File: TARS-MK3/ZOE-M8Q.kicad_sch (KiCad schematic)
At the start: 3 parts, among them U8001 ZOE-M8Q, X8001 SMACONNECTOR

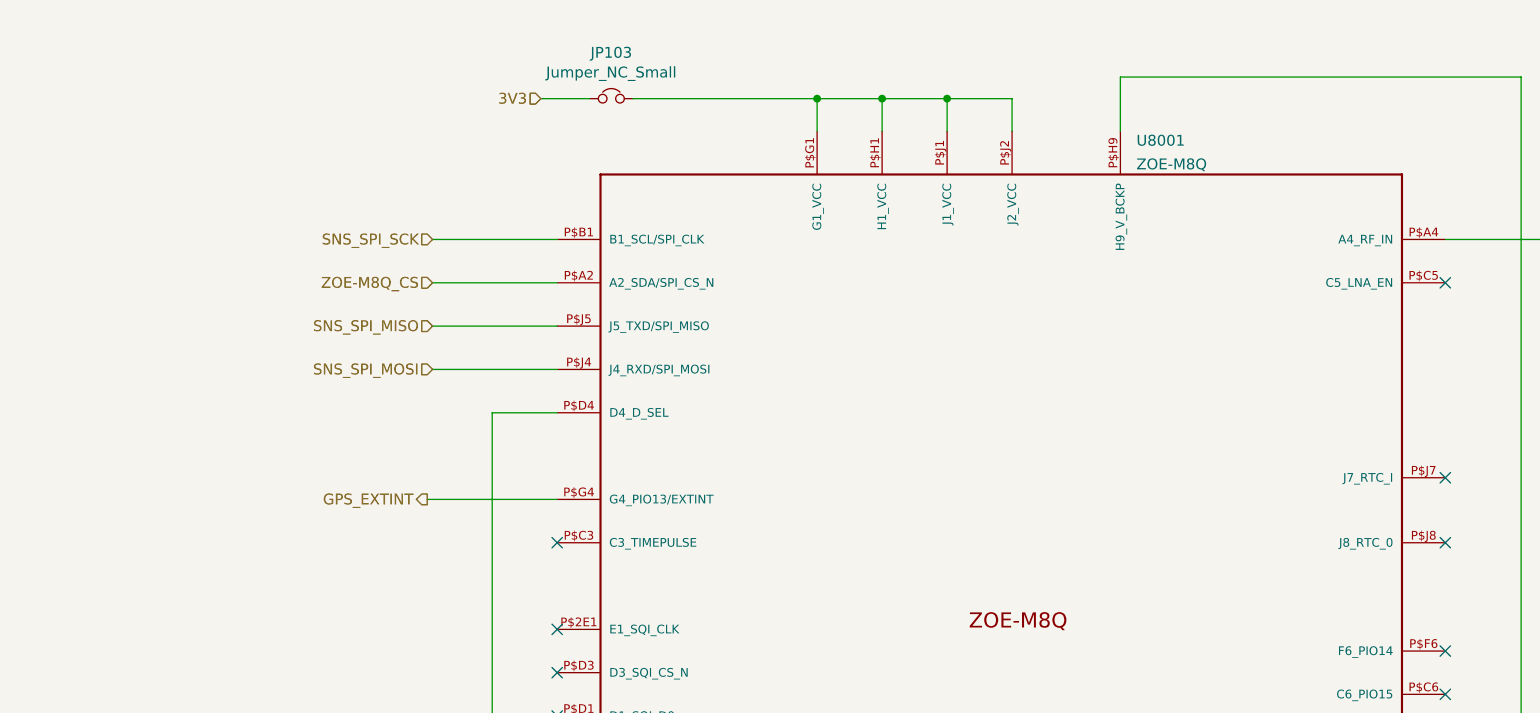
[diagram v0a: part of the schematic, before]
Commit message: added UART connections to ZOE m8q and slightly changed sensor suite pinout, also added 3V battery backup option should we want it
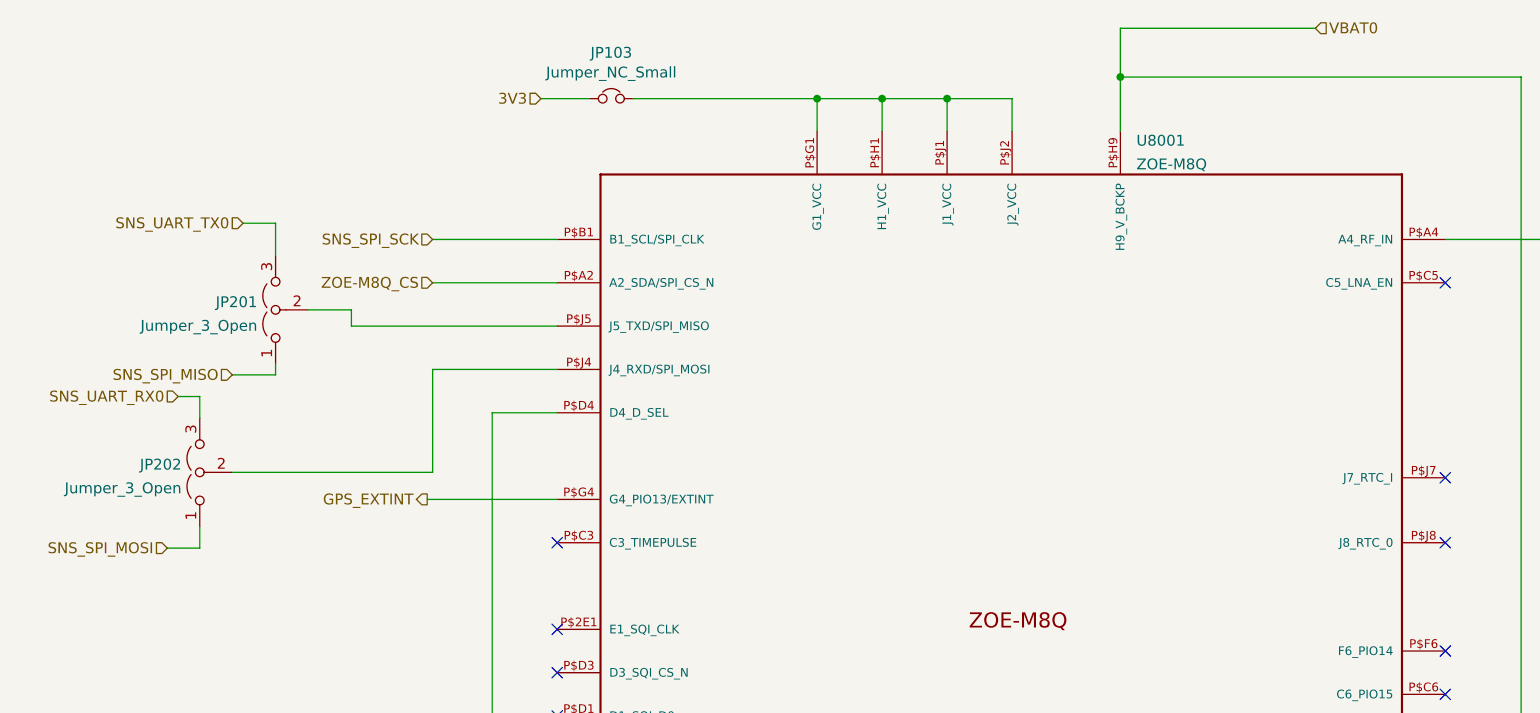
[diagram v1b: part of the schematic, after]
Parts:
- added JP201, JP202: Jumper_3_Open, Jumper:SolderJumper-3_P1.3mm_Open_RoundedPad1.0x1.5mm, symbol Jumper:Jumper_3_Open
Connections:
- net SNS_SPI_MISO: now also JP201.1 (A); no longer U8001.P$J5 (J5_TXD/SPI_MISO)
- net SNS_SPI_MOSI: now also JP202.1 (A); no longer U8001.P$J4 (J4_RXD/SPI_MOSI)
- net VBAT0: now reaches U8001.P$G9 (G9_RESERVED), U8001.P$H9 (H9_V_BCKP)
- new net: JP202.2 (C), U8001.P$J4 (J4_RXD/SPI_MOSI)
- new net: JP201.2 (C), U8001.P$J5 (J5_TXD/SPI_MISO)
- new net SNS_UART_RX0: JP202.3 (B)
- new net SNS_UART_TX0: JP201.3 (B)
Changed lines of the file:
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@@
   (junction (at 111.76 168.275) (diameter 0) (color 0 0 0 0)
+  )
+  (junction (at 137.16 29.845) (diameter 0) (color 0 0 0 0)
   )
   (junction (at 116.84 32.385) (diameter 0) (color 0 0 0 0)
@@
     (stroke (width 0) (type default) (color 0 0 0 0))
   )
+  (wire (pts (xy 142.24 160.655) (xy 142.24 168.275))
+    (stroke (width 0) (type default) (color 0 0 0 0))
+  )
+  (wire (pts (xy 71.12 59.055) (xy 46.99 59.055))
+    (stroke (width 0) (type default) (color 0 0 0 0))
+  )
+  (wire (pts (xy 137.16 29.845) (xy 184.15 29.845))
+    (stroke (width 0) (type default) (color 0 0 0 0))
+  )
+  (wire (pts (xy 167.64 168.275) (xy 167.64 160.655))
+    (stroke (width 0) (type default) (color 0 0 0 0))
+  )
+  (wire (pts (xy 101.6 168.275) (xy 106.68 168.275))
+    (stroke (width 0) (type default) (color 0 0 0 0))
+  )
+  (wire (pts (xy 71.12 53.975) (xy 56.515 53.975))
+    (stroke (width 0) (type default) (color 0 0 0 0))
+  )
+  (wire (pts (xy 203.835 56.515) (xy 206.375 56.515))
+    (stroke (width 0) (type default) (color 0 0 0 0))
+  )
+  (wire (pts (xy 184.15 29.845) (xy 184.15 127.635))
+    (stroke (width 0) (type default) (color 0 0 0 0))
+  )
+  (wire (pts (xy 63.5 168.275) (xy 81.28 168.275))
+    (stroke (width 0) (type default) (color 0 0 0 0))
+  )
   (wire (pts (xy 56.515 64.135) (xy 71.12 64.135))
     (stroke (width 0) (type default) (color 0 0 0 0))
   )
-  (wire (pts (xy 142.24 160.655) (xy 142.24 168.275))
-    (stroke (width 0) (type default) (color 0 0 0 0))
-  )
-  (wire (pts (xy 137.16 29.845) (xy 184.15 29.845))
-    (stroke (width 0) (type default) (color 0 0 0 0))
-  )
-  (wire (pts (xy 167.64 168.275) (xy 167.64 160.655))
-    (stroke (width 0) (type default) (color 0 0 0 0))
-  )
-  (wire (pts (xy 101.6 168.275) (xy 106.68 168.275))
-    (stroke (width 0) (type default) (color 0 0 0 0))
-  )
-  (wire (pts (xy 71.12 53.975) (xy 56.515 53.975))
-    (stroke (width 0) (type default) (color 0 0 0 0))
-  )
-  (wire (pts (xy 203.835 56.515) (xy 206.375 56.515))
-    (stroke (width 0) (type default) (color 0 0 0 0))
-  )
-  (wire (pts (xy 184.15 29.845) (xy 184.15 127.635))
-    (stroke (width 0) (type default) (color 0 0 0 0))
-  )
-  (wire (pts (xy 63.5 168.275) (xy 81.28 168.275))
-    (stroke (width 0) (type default) (color 0 0 0 0))
-  )
   (wire (pts (xy 91.44 160.655) (xy 91.44 168.275))
     (stroke (width 0) (type default) (color 0 0 0 0))
@@
     (stroke (width 0) (type default) (color 0 0 0 0))
   )
+  (wire (pts (xy 38.1 64.77) (xy 33.02 64.77))
+    (stroke (width 0) (type default) (color 0 0 0 0))
+  )
+  (wire (pts (xy 29.21 82.55) (xy 29.21 85.09))
+    (stroke (width 0) (type default) (color 0 0 0 0))
+  )
   (wire (pts (xy 121.92 168.275) (xy 127 168.275))
     (stroke (width 0) (type default) (color 0 0 0 0))
@@
     (stroke (width 0) (type default) (color 0 0 0 0))
   )
+  (wire (pts (xy 38.1 46.99) (xy 34.29 46.99))
+    (stroke (width 0) (type default) (color 0 0 0 0))
+  )
   (wire (pts (xy 121.92 160.655) (xy 121.92 168.275))
     (stroke (width 0) (type default) (color 0 0 0 0))
@@
     (stroke (width 0) (type default) (color 0 0 0 0))
   )
-  (wire (pts (xy 137.16 36.195) (xy 137.16 29.845))
-    (stroke (width 0) (type default) (color 0 0 0 0))
-  )
   (wire (pts (xy 201.295 41.275) (xy 203.835 41.275))
     (stroke (width 0) (type default) (color 0 0 0 0))
@@
     (stroke (width 0) (type default) (color 0 0 0 0))
   )
+  (wire (pts (xy 38.1 63.5) (xy 38.1 64.77))
+    (stroke (width 0) (type default) (color 0 0 0 0))
+  )
   (wire (pts (xy 137.16 168.275) (xy 142.24 168.275))
     (stroke (width 0) (type default) (color 0 0 0 0))
@@
     (stroke (width 0) (type default) (color 0 0 0 0))
   )
-  (wire (pts (xy 56.515 59.055) (xy 71.12 59.055))
+  (wire (pts (xy 137.16 24.13) (xy 137.16 29.845))
+    (stroke (width 0) (type default) (color 0 0 0 0))
+  )
+  (wire (pts (xy 33.02 76.2) (xy 56.515 76.2))
     (stroke (width 0) (type default) (color 0 0 0 0))
   )
@@
     (stroke (width 0) (type default) (color 0 0 0 0))
   )
+  (wire (pts (xy 38.1 50.8) (xy 38.1 46.99))
+    (stroke (width 0) (type default) (color 0 0 0 0))
+  )
   (wire (pts (xy 157.48 160.655) (xy 157.48 168.275))
     (stroke (width 0) (type default) (color 0 0 0 0))
@@
     (stroke (width 0) (type default) (color 0 0 0 0))
   )
+  (wire (pts (xy 137.16 29.845) (xy 137.16 36.195))
+    (stroke (width 0) (type default) (color 0 0 0 0))
+  )
   (wire (pts (xy 127 168.275) (xy 132.08 168.275))
     (stroke (width 0) (type default) (color 0 0 0 0))
@@
     (stroke (width 0) (type default) (color 0 0 0 0))
   )
+  (wire (pts (xy 46.99 59.055) (xy 46.99 57.15))
+    (stroke (width 0) (type default) (color 0 0 0 0))
+  )
   (wire (pts (xy 109.22 36.195) (xy 109.22 32.385))
     (stroke (width 0) (type default) (color 0 0 0 0))
   )
+  (wire (pts (xy 46.99 57.15) (xy 41.91 57.15))
+    (stroke (width 0) (type default) (color 0 0 0 0))
+  )
   (wire (pts (xy 96.52 168.275) (xy 101.6 168.275))
     (stroke (width 0) (type default) (color 0 0 0 0))
@@
     (stroke (width 0) (type default) (color 0 0 0 0))
   )
+  (wire (pts (xy 29.21 85.09) (xy 25.4 85.09))
+    (stroke (width 0) (type default) (color 0 0 0 0))
+  )
   (wire (pts (xy 71.12 69.215) (xy 63.5 69.215))
     (stroke (width 0) (type default) (color 0 0 0 0))
   )
+  (wire (pts (xy 26.67 67.31) (xy 29.21 67.31))
+    (stroke (width 0) (type default) (color 0 0 0 0))
+  )
   (wire (pts (xy 116.84 32.385) (xy 109.22 32.385))
     (stroke (width 0) (type default) (color 0 0 0 0))
@@
     (stroke (width 0) (type default) (color 0 0 0 0))
   )
+  (wire (pts (xy 29.21 67.31) (xy 29.21 69.85))
+    (stroke (width 0) (type default) (color 0 0 0 0))
+  )
   (wire (pts (xy 74.93 32.385) (xy 69.215 32.385))
     (stroke (width 0) (type default) (color 0 0 0 0))
@@
     (stroke (width 0) (type default) (color 0 0 0 0))
   )
+  (wire (pts (xy 160.02 24.13) (xy 137.16 24.13))
+    (stroke (width 0) (type default) (color 0 0 0 0))
+  )
   (wire (pts (xy 152.4 160.655) (xy 152.4 168.275))
     (stroke (width 0) (type default) (color 0 0 0 0))
@@
     (stroke (width 0) (type default) (color 0 0 0 0))
   )
+  (wire (pts (xy 56.515 76.2) (xy 56.515 64.135))
+    (stroke (width 0) (type default) (color 0 0 0 0))
+  )
   (wire (pts (xy 121.92 172.085) (xy 121.92 168.275))
     (stroke (width 0) (type default) (color 0 0 0 0))
@@
     (effects (font (size 1.27 1.27)) (justify right))
   )
+  (hierarchical_label "VBAT0" (shape input) (at 160.02 24.13 0)
+    (effects (font (size 1.27 1.27)) (justify left))
+  )
   (hierarchical_label "3V3" (shape input) (at 69.215 32.385 180)
     (effects (font (size 1.27 1.27)) (justify right))
   )
-  (hierarchical_label "SNS_SPI_MISO" (shape input) (at 56.515 59.055 180)
-    (effects (font (size 1.27 1.27)) (justify right))
-  )
-  (hierarchical_label "SNS_SPI_MOSI" (shape input) (at 56.515 64.135 180)
+  (hierarchical_label "SNS_SPI_MISO" (shape input) (at 33.02 64.77 180)
+    (effects (font (size 1.27 1.27)) (justify right))
+  )
+  (hierarchical_label "SNS_UART_TX0" (shape input) (at 34.29 46.99 180)
+    (effects (font (size 1.27 1.27)) (justify right))
+  )
+  (hierarchical_label "SNS_SPI_MOSI" (shape input) (at 25.4 85.09 180)
     (effects (font (size 1.27 1.27)) (justify right))
   )
   (hierarchical_label "SNS_SPI_SCK" (shape input) (at 56.515 48.895 180)
+    (effects (font (size 1.27 1.27)) (justify right))
+  )
+  (hierarchical_label "SNS_UART_RX0" (shape input) (at 26.67 67.31 180)
     (effects (font (size 1.27 1.27)) (justify right))
   )
@@
     )
     (pin "1")
+  )
+  (symbol (lib_id "Jumper:Jumper_3_Open") (at 29.21 76.2 90) (unit 1)
+    (in_bom yes) (on_board yes) (fields_autoplaced)
+    (property "Reference" "JP202" (id 0) (at 27.0759 75.2915 90)
+      (effects (font (size 1.27 1.27)) (justify left))
+    )
+    (property "Value" "Jumper_3_Open" (id 1) (at 27.0759 78.0666 90)
+      (effects (font (size 1.27 1.27)) (justify left))
+    )
+    (property "Footprint" "Jumper:SolderJumper-3_P1.3mm_Open_RoundedPad1.0x1.5mm" (id 2) (at 29.21 76.2 0)
+      (effects (font (size 1.27 1.27)) hide)
+    )
+    (property "Datasheet" "~" (id 3) (at 29.21 76.2 0)
+      (effects (font (size 1.27 1.27)) hide)
+    )
+    (pin "1")
+    (pin "2")
+    (pin "3")
   )
   (symbol (lib_id "ZOE-M8Q:ZOE-M8Q") (at 147.32 130.175 0) (unit 1)
@@
     (pin "GND4")
   )
+  (symbol (lib_id "Jumper:Jumper_3_Open") (at 38.1 57.15 90) (unit 1)
+    (in_bom yes) (on_board yes) (fields_autoplaced)
+    (property "Reference" "JP201" (id 0) (at 35.9659 56.2415 90)
+      (effects (font (size 1.27 1.27)) (justify left))
+    )
+    (property "Value" "Jumper_3_Open" (id 1) (at 35.9659 59.0166 90)
+      (effects (font (size 1.27 1.27)) (justify left))
+    )
+    (property "Footprint" "Jumper:SolderJumper-3_P1.3mm_Open_RoundedPad1.0x1.5mm" (id 2) (at 38.1 57.15 0)
+      (effects (font (size 1.27 1.27)) hide)
+    )
+    (property "Datasheet" "~" (id 3) (at 38.1 57.15 0)
+      (effects (font (size 1.27 1.27)) hide)
+    )
+    (pin "1")
+    (pin "2")
+    (pin "3")
+  )
   (sheet_instances

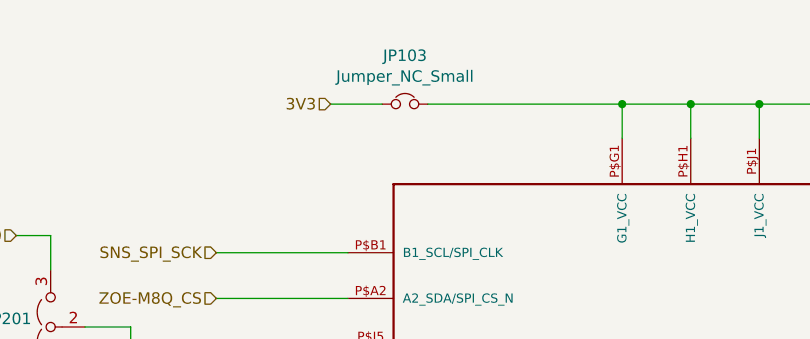
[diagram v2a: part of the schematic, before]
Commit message: Starting routing
Starting routing
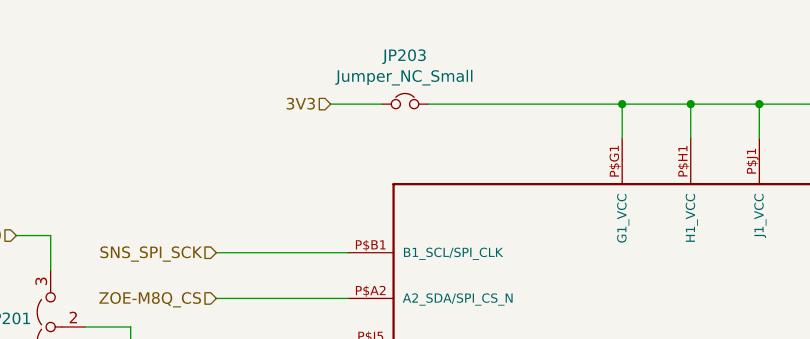
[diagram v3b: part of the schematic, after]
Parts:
- renumbered JP103 to JP203
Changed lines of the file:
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@@
   (symbol (lib_id "Device:Jumper_NC_Small") (at 77.47 32.385 0) (unit 1)
     (in_bom yes) (on_board yes)
-    (property "Reference" "JP103" (id 0) (at 77.47 27.0002 0))
+    (property "Reference" "JP203" (id 0) (at 77.47 27.0002 0))
     (property "Value" "Jumper_NC_Small" (id 1) (at 77.47 29.3116 0))
     (property "Footprint" "Jumper:SolderJumper-2_P1.3mm_Bridged2Bar_RoundedPad1.0x1.5mm" (id 2) (at 77.47 32.385 0)

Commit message: Add ZOE-M8Q footprint to Sensor Suite
Add ZOE-M8Q footprint to Sensor Suite
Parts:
- U8001: footprint ZOE-M8 -> ZOE-M8Q:ZOE-M8Q
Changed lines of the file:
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@@
       (effects (font (size 1.27 1.27)) (justify left))
     )
-    (property "Footprint" "ZOE-M8" (id 2) (at 147.32 130.175 0)
+    (property "Footprint" "ZOE-M8Q:ZOE-M8Q" (id 2) (at 147.32 130.175 0)
       (effects (font (size 1.27 1.27)) (justify left bottom) hide)
     )
@@
       (reference "#PWR0203") (unit 1) (value "GND") (footprint "")
     )
+    (path "/ec6852de-4231-4fe1-9566-484449f4d321"
+      (reference "JP201") (unit 1) (value "Jumper_3_Open") (footprint "Jumper:SolderJumper-3_P1.3mm_Open_RoundedPad1.0x1.5mm")
+    )
+    (path "/00a97a41-2aea-4ea5-b50e-8ecdd4ade130"
+      (reference "JP202") (unit 1) (value "Jumper_3_Open") (footprint "Jumper:SolderJumper-3_P1.3mm_Open_RoundedPad1.0x1.5mm")
+    )
     (path "/00000000-0000-0000-0000-000061cc37df"
-      (reference "JP103") (unit 1) (value "Jumper_NC_Small") (footprint "Jumper:SolderJumper-2_P1.3mm_Bridged2Bar_RoundedPad1.0x1.5mm")
+      (reference "JP203") (unit 1) (value "Jumper_NC_Small") (footprint "Jumper:SolderJumper-2_P1.3mm_Bridged2Bar_RoundedPad1.0x1.5mm")
     )
     (path "/6c9a076d-21ce-48cc-a4d7-55822e95fa95"
-      (reference "U8001") (unit 1) (value "ZOE-M8Q") (footprint "ZOE-M8")
+      (reference "U8001") (unit 1) (value "ZOE-M8Q") (footprint "ZOE-M8Q:ZOE-M8Q")
     )
     (path "/8f0e1ea6-d278-4117-9e02-aaadcc59362e"

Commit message: added uFL footprint from adafruit breakout
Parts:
- X8001: footprint (none) -> uFL:uFL
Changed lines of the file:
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@@
   (symbol (lib_id "power:GND") (at 121.92 172.085 0) (unit 1)
     (in_bom yes) (on_board yes)
-    (property "Reference" "#PWR0201" (id 0) (at 121.92 178.435 0)
+    (property "Reference" "#PWR0110" (id 0) (at 121.92 178.435 0)
       (effects (font (size 1.27 1.27)) hide)
     )
@@
   (symbol (lib_id "power:GND") (at 203.835 60.96 0) (unit 1)
     (in_bom yes) (on_board yes)
-    (property "Reference" "#PWR0203" (id 0) (at 203.835 67.31 0)
+    (property "Reference" "#PWR0111" (id 0) (at 203.835 67.31 0)
       (effects (font (size 1.27 1.27)) hide)
     )
@@
   (symbol (lib_id "power:GND") (at 203.835 38.735 180) (unit 1)
     (in_bom yes) (on_board yes)
-    (property "Reference" "#PWR0202" (id 0) (at 203.835 32.385 0)
+    (property "Reference" "#PWR0112" (id 0) (at 203.835 32.385 0)
       (effects (font (size 1.27 1.27)) hide)
     )
@@
       (effects (font (size 1.27 1.27)) (justify left))
     )
-    (property "Footprint" "" (id 2) (at 203.835 48.895 0)
+    (property "Footprint" "uFL:uFL" (id 2) (at 203.835 48.895 0)
       (effects (font (size 1.27 1.27)) hide)
     )
